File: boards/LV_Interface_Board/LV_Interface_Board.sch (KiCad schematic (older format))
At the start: 15 parts, among them J1 Ampseal_35, J2 Ampseal_35, J3 micromatch_male_6, J4 micromatch_male_20, J5 micromatch_male_20, J6 micromatch_male_12, J7 micromatch_male_18, J8 micromatch_male_20, J9 micromatch_male_20, SW1 3P4T_rotary_switch, U1 RJ45_VT

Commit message: checking off lv interface sch
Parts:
- added C1: C_10uF, footprints:C_0805_OEM, symbol C_10uF
- added D4: LED_0805, footprints:LED_0805_OEM, symbol LED_0805
- added LED1, LED2: SEGMENT_12BAR_BICOLOR, adafruit:SEGMENT_BICOL_BL-AR12Z3010, symbol SEGMENT_12BAR_BICOLOR
- added R1: R_500, footprints:R_0805_OEM, symbol R_500
- added R2, R3: R_10k, footprints:R_0805_OEM, symbol R_10k
- added U2: HT16K33, footprints:SOP28, symbol HT16K33
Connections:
- net BRAKE_LIGHT_12V is gone; now on net 12V: J1.9
- net BSPD_SHUTDOWN_IN is gone; now on net RIGHT_E-STOP: J8.10, J8.11, J8.12, J8.7, J8.8, J8.9
- net 12V: now also F1.2 (out)
- net 5V: now also C1.1, R1.1, R2.1, R3.1, U2.28 (VDD)
- net COOLING_PUMP_12V_FUSED: now also F1.4 (out); no longer F1.1 (in)
- net GLVMS: now also F1.1 (in), F1.5 (in)
- net GND: now also C1.2, D4.1 (K), U2.1 (VSS)
- net MAIN_SHUTDOWN_FUSE: now also F1.6 (out)
- net SCL: now also R3.2, U2.26 (SCL)
- net SDA: now also R2.2, U2.27 (SDA)
- new net: D4.2 (A), R1.2
- new net COM0: LED1.1 (A1), LED1.14 (A2), LED2.1 (A1), LED2.14 (A2), U2.2 (COM0/AD)
- new net COM1: LED1.6 (A3), LED1.9 (A4), LED2.6 (A3), LED2.9 (A4), U2.3 (COM1/KS0)
- new net COM2: LED1.7 (A5), LED1.8 (A6), LED2.7 (A5), LED2.8 (A6), U2.4 (COM2/KS1)
- new net ROW0: LED2.2 (K1), U2.25 (ROW0/A2)
- new net ROW1: LED2.3 (K3), U2.24 (ROW1/A1)
- new net ROW10: LED2.11 (K6), U2.15 (ROW10/K8)
- new net ROW11: LED2.10 (K8), U2.14 (ROW11/K9)
- new net ROW12: LED1.13 (K2), U2.13 (ROW12/K10)
- new net ROW13: LED1.12 (K4), U2.12 (ROW13/K11)
- new net ROW14: LED1.11 (K6), U2.11 (ROW14/K12)
- new net ROW15: LED1.10 (K8), U2.10 (ROW15/K13/INT)
- new net ROW2: LED2.4 (K5), U2.23 (ROW2/A0)
- new net ROW3: LED2.5 (K7), U2.22 (ROW3/K1)
- new net ROW4: LED1.2 (K1), U2.21 (ROW4/K2)
- new net ROW5: LED1.3 (K3), U2.20 (ROW5/K3)
- new net ROW6: LED1.4 (K5), U2.19 (ROW6/K4)
- new net ROW7: LED1.5 (K7), U2.18 (ROW7/K5)
- new net ROW8: LED2.13 (K2), U2.17 (ROW8/K6)
- new net ROW9: LED2.12 (K4), U2.16 (ROW9/K7)
- no-connect marks 28 -> 32
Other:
- note added: "Ampseals\n"
- note added: "BSPD shutdown in\n"
- note added: "Going to brake light (outside of car)"
- note added: "LED Status Bar\n"
- note removed: "Actual light, not the board"
- moved on the sheet: D1, D2, D3, F1, J1, J2, J3, J4, J5, J6, J7, J8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

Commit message: updated footprint matching, schematic fully checked off
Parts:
- J3: footprint (none) -> footprints:micromatch_female_ra_6
- J4, J5, J8, J9: footprint (none) -> footprints:micromatch_female_ra_20
- J6: footprint (none) -> footprints:micromatch_female_ra_12
- J7: footprint (none) -> footprints:micromatch_female_ra_18
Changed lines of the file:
@@
 LIBS:switches
 LIBS:relays
+LIBS:motors
 LIBS:transistors
 LIBS:conn
@@
 LIBS:formula
 LIBS:LV_Interface_Board-cache
-LIBS:Backpack-cache
 EELAYER 25 0
 EELAYER END
@@
 F 0 "J6" H 8110 13050 60  0000 C CNN
 F 1 "micromatch_male_12" H 8160 11750 60  0000 C CNN
-F 2 "" H 8010 12950 60  0001 C CNN
+F 2 "footprints:micromatch_female_ra_12" H 8010 12950 60  0001 C CNN
 F 3 "" H 8110 13050 60  0001 C CNN
 F 4 "A110882CT-ND" H 8160 12650 60  0001 C CNN "MPN"
@@
 F 0 "J7" H 8110 14650 60  0000 C CNN
 F 1 "micromatch_male_18" H 8160 12750 60  0000 C CNN
-F 2 "" H 8010 14550 60  0001 C CNN
+F 2 "footprints:micromatch_female_ra_18" H 8010 14550 60  0001 C CNN
 F 3 "" H 8110 14650 60  0001 C CNN
 F 4 "A110884CT-ND" H 8210 13450 60  0001 C CNN "MPN"
@@
 F 0 "J5" H 5115 13255 60  0000 C CNN
 F 1 "micromatch_male_20" H 5165 11155 60  0000 C CNN
-F 2 "" H 5015 13155 60  0001 C CNN
+F 2 "footprints:micromatch_female_ra_20" H 5015 13155 60  0001 C CNN
 F 3 "" H 5115 13255 60  0001 C CNN
 F 4 "A111126CT-ND" H 5215 12055 60  0001 C CNN "MPN"
@@
 F 0 "J8" H 11480 13085 60  0000 C CNN
 F 1 "micromatch_male_20" H 11530 10985 60  0000 C CNN
-F 2 "" H 11380 12985 60  0001 C CNN
+F 2 "footprints:micromatch_female_ra_20" H 11380 12985 60  0001 C CNN
 F 3 "" H 11480 13085 60  0001 C CNN
 F 4 "A111126CT-ND" H 11580 11885 60  0001 C CNN "MPN"
@@
 F 0 "J4" H 2240 13050 60  0000 C CNN
 F 1 "micromatch_male_20" H 2290 10950 60  0000 C CNN
-F 2 "" H 2140 12950 60  0001 C CNN
+F 2 "footprints:micromatch_female_ra_20" H 2140 12950 60  0001 C CNN
 F 3 "" H 2240 13050 60  0001 C CNN
 F 4 "A111126CT-ND" H 2340 11850 60  0001 C CNN "MPN"
@@
 F 0 "J3" H 2215 13725 60  0000 C CNN
 F 1 "micromatch_male_6" H 2215 13025 60  0000 C CNN
-F 2 "" H 2115 13625 60  0001 C CNN
+F 2 "footprints:micromatch_female_ra_6" H 2115 13625 60  0001 C CNN
 F 3 "" H 2215 13725 60  0001 C CNN
 F 4 "A107035CT-ND" H 2265 13325 60  0001 C CNN "MPN"
@@
 F 0 "J9" H 14250 13095 60  0000 C CNN
 F 1 "micromatch_male_20" H 14300 10995 60  0000 C CNN
-F 2 "" H 14150 12995 60  0001 C CNN
+F 2 "footprints:micromatch_female_ra_20" H 14150 12995 60  0001 C CNN
 F 3 "" H 14250 13095 60  0001 C CNN
 F 4 "A111126CT-ND" H 14350 11895 60  0001 C CNN "MPN"

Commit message: working on LV interface layout, added measurements to LV box boards to accurately place connectors
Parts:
- LED1, LED2: footprint adafruit:SEGMENT_BICOL_BL-AR12Z3010 -> footprints:SEGMENT_BICOL_BL-AR12Z3010
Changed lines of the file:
@@
 F 0 "LED2" H 13850 3065 45  0000 L BNN
 F 1 "SEGMENT_12BAR_BICOLOR" H 13850 2965 45  0000 L BNN
-F 2 "adafruit:SEGMENT_BICOL_BL-AR12Z3010" H 17350 2265 60  0001 C CNN
+F 2 "footprints:SEGMENT_BICOL_BL-AR12Z3010" H 17350 2265 60  0001 C CNN
 F 3 "" H 17350 2265 60  0001 C CNN
 	1    17350 2265
@@
 F 0 "LED1" H 13830 5255 45  0000 L BNN
 F 1 "SEGMENT_12BAR_BICOLOR" H 13830 5155 45  0000 L BNN
-F 2 "adafruit:SEGMENT_BICOL_BL-AR12Z3010" H 17330 4455 60  0001 C CNN
+F 2 "footprints:SEGMENT_BICOL_BL-AR12Z3010" H 17330 4455 60  0001 C CNN
 F 3 "" H 17330 4455 60  0001 C CNN
 	1    17330 4455

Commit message: improved routing
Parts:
- F1: PurchasingLink (none) -> https://www.digikey.com/products/en/circuit-protection/fuse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
- U1: PurchasingLink (none) -> https://www.digikey.com/products/en?keywords=MRJ-5481-01
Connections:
- net 12V: now also F1.4 (out); no longer F1.2 (out)
- net BRAKE_LIGHT_LSD: now also J1.19; no longer J1.10
- net BRAKE_SWITCH+: now also J2.11; no longer J1.11
- net BRAKE_SWITCH-: now also J2.12; no longer J1.12
- net COOLING_PUMP_12V_FUSED: now also F1.2 (out), J1.10, J1.11, J1.12; no longer F1.4 (out), J1.19
- no-connect marks 32 -> 30
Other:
- note added: "needs purchasing (led)"
- note added: "needs purchasing\n"
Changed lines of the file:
@@
 LIBS:switches
 LIBS:relays
-LIBS:motors
 LIBS:transistors
 LIBS:conn
@@
 Text Label 2105 3135 0    60   ~ 0
 12V
-Text Label 2105 3235 0    60   ~ 0
+Text Label 2105 4135 0    60   ~ 0
 BRAKE_LIGHT_LSD
-Text Label 2105 3335 0    60   ~ 0
+Text Label 5525 3355 0    60   ~ 0
 BRAKE_SWITCH+
-Text Label 2105 3435 0    60   ~ 0
+Text Label 5525 3455 0    60   ~ 0
 BRAKE_SWITCH-
 Text Label 2105 2935 0    60   ~ 0
@@
 Text Label 2105 4035 0    60   ~ 0
 CAN_LOW
-Text Label 2105 4135 0    60   ~ 0
+Text Label 2105 3335 0    60   ~ 0
 COOLING_PUMP_12V_FUSED
-NoConn ~ 5525 3355
-NoConn ~ 5525 3455
 Text Label 2105 4935 0    60   ~ 0
 BAT+
@@
 F 2 "footprints:RJ45-Vertical" H 7525 7820 60  0001 C CNN
 F 3 "" H 7625 7920 60  0001 C CNN
+F 4 "https://www.digikey.com/products/en?keywords=MRJ-5481-01" H 7625 8510 60  0001 C CNN "PurchasingLink"
 	1    7625 8510
 	1    0    0    -1
@@
 F 5 "F5764CT-ND" H 2710 7795 60  0001 C CNN "MPN"
 F 6 "Value" H 2870 8155 60  0001 C CNN "Package"
+F 7 "https://www.digikey.com/products/en/circuit-protection/fuseholders/140?k=&pkeyword=&pv2094=i4&FV=ffe0008c%2C114007b%2C1140003&mnonly=0&ColumnSort=1000011&page=1&stock=1&quantity=0&ptm=0&fid=0&pageSize=25" H 1860 8555 60  0001 C CNN "PurchasingLink"
 	1    1860 8555
 	1    0    0    -1
@@
 Text Label 1280 8415 0    60   ~ 0
 GLVMS
+Text Label 2130 8585 0    60   ~ 0
+12V
 Text Label 2130 8505 0    60   ~ 0
-12V
-Text Label 2130 8585 0    60   ~ 0
 COOLING_PUMP_12V_FUSED
 Text Label 2130 8665 0    60   ~ 0
@@
 Text Notes 12110 11690 0    60   ~ 0
 BSPD shutdown in\n
+Text Notes 11420 2340 0    60   ~ 0
+needs purchasing\n
+Text Notes 4445 2080 0    60   ~ 0
+needs purchasing\n
+Text Notes 16670 1480 0    60   ~ 0
+needs purchasing (led)
+Text Label 2105 3235 0    60   ~ 0
+COOLING_PUMP_12V_FUSED
+Text Label 2105 3435 0    60   ~ 0
+COOLING_PUMP_12V_FUSED
 $EndSCHEMATC

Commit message: saving progress before switching strain and sensor pins
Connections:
- net GAUGE2+: now also J2.6; no longer J2.30
- net GAUGE2-: now also J2.4; no longer J2.29
- net GAUGE2_MID: now also J2.5; no longer J2.18
- net GAUGE3+: now also J2.3; no longer J2.17
- net GAUGE3-: now also J2.1; no longer J2.16
- net GAUGE3_MID: now also J2.2; no longer J2.28
- net GAUGE4+: now also J2.14; no longer J2.6
- net GAUGE4-: now also J2.27; no longer J2.4
- net GAUGE4_MID: now also J2.15; no longer J2.5
- net GAUGE5+: now also J2.16; no longer J2.27
- net GAUGE5-: now also J2.17; no longer J2.14
- net GAUGE5_MID: now also J2.28; no longer J2.15
- net GAUGE6+: now also J2.29; no longer J2.3
- net GAUGE6-: now also J2.30; no longer J2.1
- net GAUGE6_MID: now also J2.18; no longer J2.2
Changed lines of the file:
@@
 Text Label 5525 2955 0    60   ~ 0
 GAUGE1-
-Text Label 5525 2855 0    60   ~ 0
+Text Label 5525 3655 0    60   ~ 0
 GAUGE4+
-Text Label 5525 2755 0    60   ~ 0
+Text Label 5525 3755 0    60   ~ 0
 GAUGE4_MID
-Text Label 5525 2655 0    60   ~ 0
+Text Label 5525 4955 0    60   ~ 0
 GAUGE4-
-Text Label 5525 2555 0    60   ~ 0
+Text Label 5525 5155 0    60   ~ 0
 GAUGE6+
-Text Label 5525 2455 0    60   ~ 0
+Text Label 5525 4055 0    60   ~ 0
 GAUGE6_MID
-Text Label 5525 2355 0    60   ~ 0
+Text Label 5525 5255 0    60   ~ 0
 GAUGE6-
 Text Label 5525 4155 0    60   ~ 0
 GAUGE1_MID
-Text Label 5525 4055 0    60   ~ 0
+Text Label 5525 2755 0    60   ~ 0
 GAUGE2_MID
+Text Label 5525 2555 0    60   ~ 0
+GAUGE3+
+Text Label 5525 2355 0    60   ~ 0
+GAUGE3-
+Text Label 5525 2855 0    60   ~ 0
+GAUGE2+
+Text Label 5525 2655 0    60   ~ 0
+GAUGE2-
+Text Label 5525 2455 0    60   ~ 0
+GAUGE3_MID
+Text Label 5525 3855 0    60   ~ 0
+GAUGE5+
 Text Label 5525 3955 0    60   ~ 0
-GAUGE3+
-Text Label 5525 3855 0    60   ~ 0
-GAUGE3-
-Text Label 5525 5255 0    60   ~ 0
-GAUGE2+
-Text Label 5525 5155 0    60   ~ 0
-GAUGE2-
+GAUGE5-
 Text Label 5525 5055 0    60   ~ 0
-GAUGE3_MID
-Text Label 5525 4955 0    60   ~ 0
-GAUGE5+
-Text Label 5525 3655 0    60   ~ 0
-GAUGE5-
-Text Label 5525 3755 0    60   ~ 0
 GAUGE5_MID
 Text Label 5365 12055 0    60   ~ 0

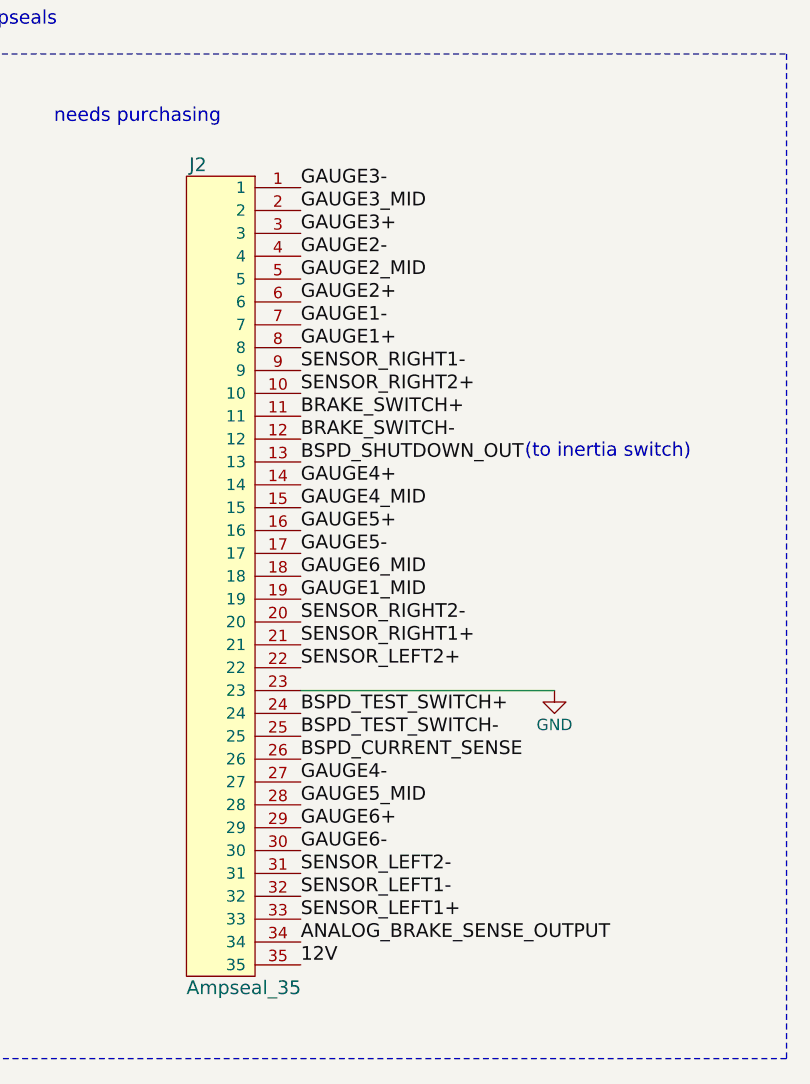
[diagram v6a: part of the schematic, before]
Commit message: shifted sensor and gauge pins around on Ampseal 2
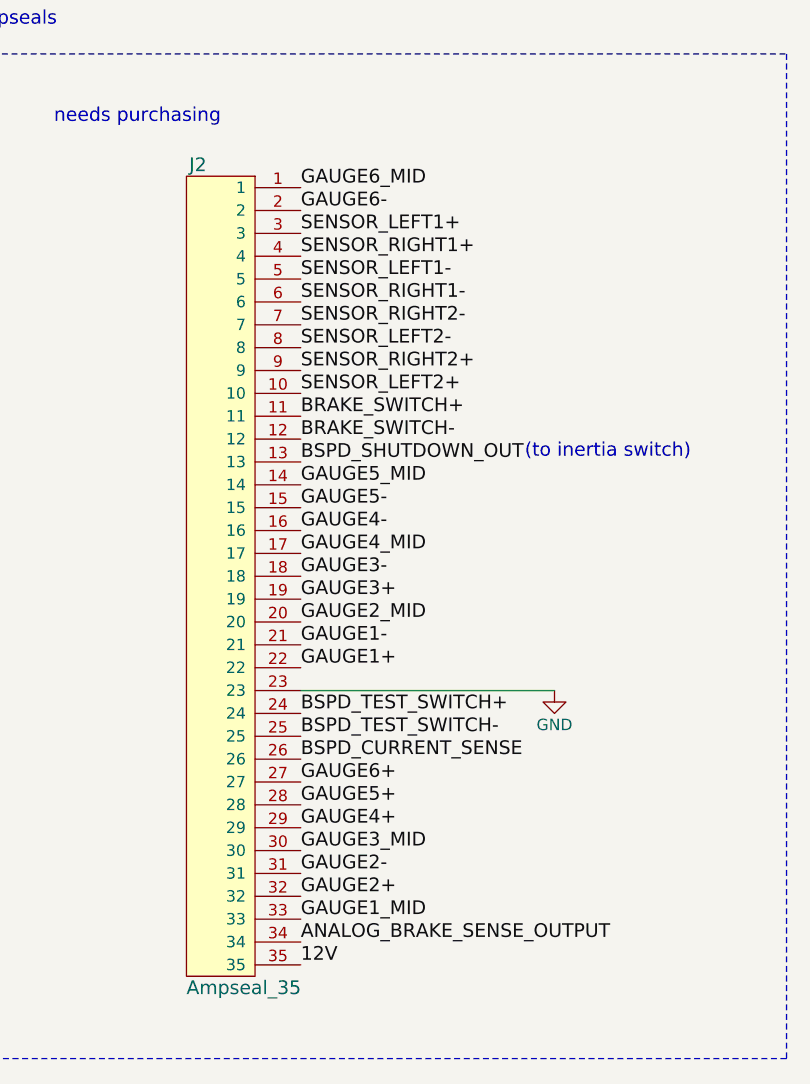
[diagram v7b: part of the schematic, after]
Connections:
- net GAUGE1+: now also J2.22; no longer J2.8
- net GAUGE1-: now also J2.21; no longer J2.7
- net GAUGE1_MID: now also J2.33; no longer J2.19
- net GAUGE2+: now also J2.32; no longer J2.6
- net GAUGE2-: now also J2.31; no longer J2.4
- net GAUGE2_MID: now also J2.20; no longer J2.5
- net GAUGE3+: now also J2.19; no longer J2.3
- net GAUGE3-: now also J2.18; no longer J2.1
- net GAUGE3_MID: now also J2.30; no longer J2.2
- net GAUGE4+: now also J2.29; no longer J2.14
- net GAUGE4-: now also J2.16; no longer J2.27
- net GAUGE4_MID: now also J2.17; no longer J2.15
- net GAUGE5+: now also J2.28; no longer J2.16
- net GAUGE5-: now also J2.15; no longer J2.17
- net GAUGE5_MID: now also J2.14; no longer J2.28
- net GAUGE6+: now also J2.27; no longer J2.29
- net GAUGE6-: now also J2.2; no longer J2.30
- net GAUGE6_MID: now also J2.1; no longer J2.18
- net SENSOR_LEFT1+: now also J2.3; no longer J2.33
- net SENSOR_LEFT1-: now also J2.5; no longer J2.32
- net SENSOR_LEFT2+: now also J2.10; no longer J2.22
- net SENSOR_LEFT2-: now also J2.8; no longer J2.31
- net SENSOR_RIGHT1+: now also J2.4; no longer J2.21
- net SENSOR_RIGHT1-: now also J2.6; no longer J2.9
- net SENSOR_RIGHT2+: now also J2.9; no longer J2.10
- net SENSOR_RIGHT2-: now also J2.7; no longer J2.20
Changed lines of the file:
@@
 Text Notes 7965 7680 2    60   ~ 0
 External RJ45\n
-Text Label 5525 3055 0    60   ~ 0
+Text Label 5525 4455 0    60   ~ 0
 GAUGE1+
-Text Label 5525 2955 0    60   ~ 0
+Text Label 5525 4355 0    60   ~ 0
 GAUGE1-
+Text Label 5525 5155 0    60   ~ 0
+GAUGE4+
+Text Label 5525 3955 0    60   ~ 0
+GAUGE4_MID
+Text Label 5525 3855 0    60   ~ 0
+GAUGE4-
+Text Label 5525 4955 0    60   ~ 0
+GAUGE6+
+Text Label 5525 2355 0    60   ~ 0
+GAUGE6_MID
+Text Label 5525 2455 0    60   ~ 0
+GAUGE6-
+Text Label 5525 5555 0    60   ~ 0
+GAUGE1_MID
+Text Label 5525 4255 0    60   ~ 0
+GAUGE2_MID
+Text Label 5525 4155 0    60   ~ 0
+GAUGE3+
+Text Label 5525 4055 0    60   ~ 0
+GAUGE3-
+Text Label 5525 5455 0    60   ~ 0
+GAUGE2+
+Text Label 5525 5355 0    60   ~ 0
+GAUGE2-
+Text Label 5525 5255 0    60   ~ 0
+GAUGE3_MID
+Text Label 5525 5055 0    60   ~ 0
+GAUGE5+
+Text Label 5525 3755 0    60   ~ 0
+GAUGE5-
 Text Label 5525 3655 0    60   ~ 0
-GAUGE4+
-Text Label 5525 3755 0    60   ~ 0
-GAUGE4_MID
-Text Label 5525 4955 0    60   ~ 0
-GAUGE4-
-Text Label 5525 5155 0    60   ~ 0
-GAUGE6+
-Text Label 5525 4055 0    60   ~ 0
-GAUGE6_MID
-Text Label 5525 5255 0    60   ~ 0
-GAUGE6-
-Text Label 5525 4155 0    60   ~ 0
-GAUGE1_MID
-Text Label 5525 2755 0    60   ~ 0
-GAUGE2_MID
-Text Label 5525 2555 0    60   ~ 0
-GAUGE3+
-Text Label 5525 2355 0    60   ~ 0
-GAUGE3-
-Text Label 5525 2855 0    60   ~ 0
-GAUGE2+
-Text Label 5525 2655 0    60   ~ 0
-GAUGE2-
-Text Label 5525 2455 0    60   ~ 0
-GAUGE3_MID
-Text Label 5525 3855 0    60   ~ 0
-GAUGE5+
-Text Label 5525 3955 0    60   ~ 0
-GAUGE5-
-Text Label 5525 5055 0    60   ~ 0
 GAUGE5_MID
 Text Label 5365 12055 0    60   ~ 0
@@
 Text Label 5365 12755 0    60   ~ 0
 SENSOR_RIGHT2-
-Text Label 5525 5555 0    60   ~ 0
+Text Label 5525 2555 0    60   ~ 0
 SENSOR_LEFT1+
-Text Label 5525 5455 0    60   ~ 0
+Text Label 5525 2755 0    60   ~ 0
 SENSOR_LEFT1-
-Text Label 5525 4455 0    60   ~ 0
+Text Label 5525 3255 0    60   ~ 0
 SENSOR_LEFT2+
-Text Label 5525 5355 0    60   ~ 0
+Text Label 5525 3055 0    60   ~ 0
 SENSOR_LEFT2-
-Text Label 5525 4355 0    60   ~ 0
+Text Label 5525 2655 0    60   ~ 0
 SENSOR_RIGHT1+
+Text Label 5525 2855 0    60   ~ 0
+SENSOR_RIGHT1-
 Text Label 5525 3155 0    60   ~ 0
-SENSOR_RIGHT1-
-Text Label 5525 3255 0    60   ~ 0
 SENSOR_RIGHT2+
-Text Label 5525 4255 0    60   ~ 0
+Text Label 5525 2955 0    60   ~ 0
 SENSOR_RIGHT2-
 Text Label 5525 4855 0    60   ~ 0
